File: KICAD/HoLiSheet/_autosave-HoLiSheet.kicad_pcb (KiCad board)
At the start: 2 copper layers, 22.4 x 31.4 mm, 13 parts, among them J1 Conn_01x06, J2 Conn_01x01_Male, J3 Conn_01x06, J4 Conn_01x01_Male, J5 Conn_01x01_Male, J6 Conn_01x01_Male, J7 Conn_01x01_Male, J8 Conn_01x01_Male

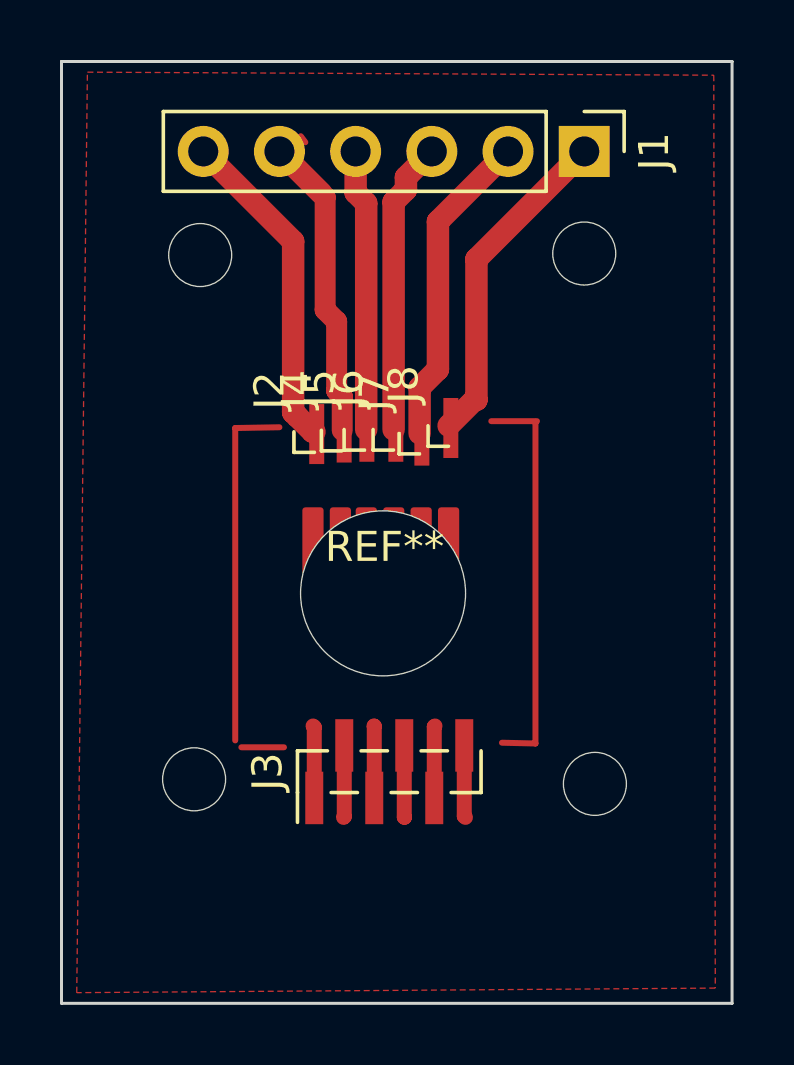
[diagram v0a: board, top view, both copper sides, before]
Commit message: Adding new standalone CAD and new iamges
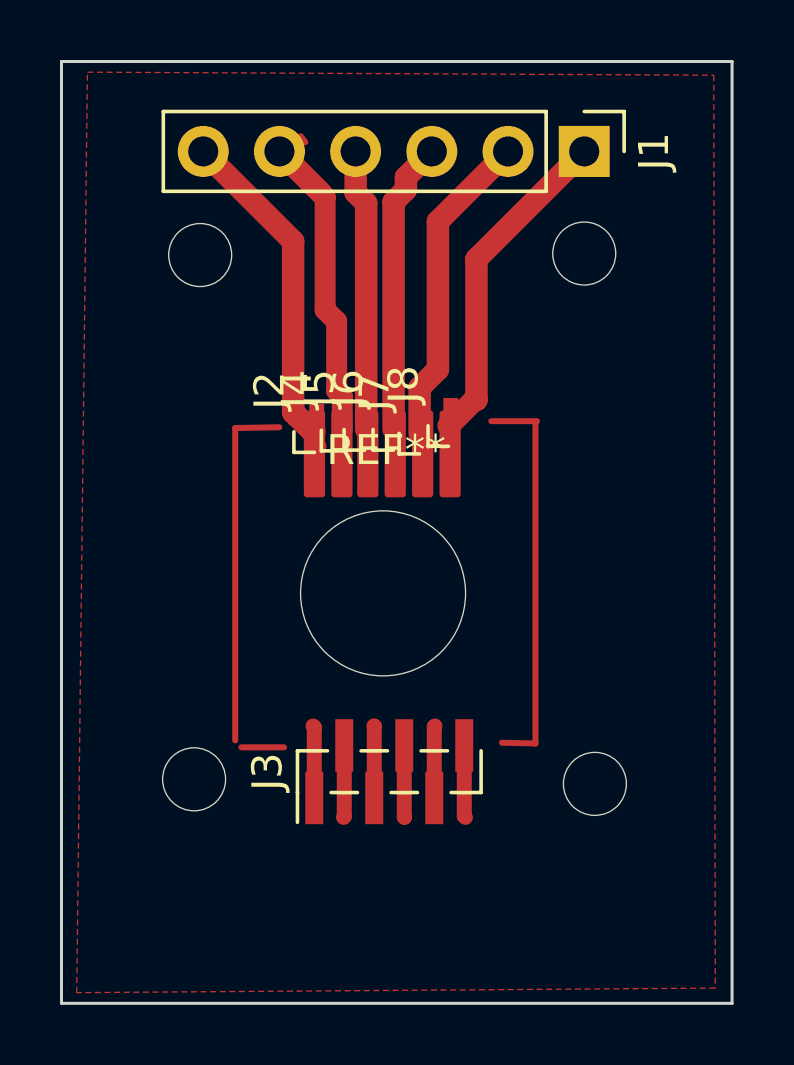
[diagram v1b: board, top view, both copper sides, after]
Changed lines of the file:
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@@
     (tags "mounting hole 5.5mm no annular")
     (attr exclude_from_pos_files exclude_from_bom)
-    (fp_text reference "REF**" (at 0.0508 -1.547) (layer "F.SilkS")
+    (fp_text reference "REF**" (at 0.1016 -4.7728) (layer "F.SilkS")
       (effects (font (size 1 1) (thickness 0.15)))
     )
@@
   (gr_line (start 16.002 12.1666) (end 16.002 22.8854) (layer "F.Cu") (width 0.2))
   (gr_line (start 16.002 22.8854) (end 14.8844 22.86) (layer "F.Cu") (width 0.2))
-  (gr_rect (start 10.6172 15.113) (end 10.1092 17.8054) (layer "F.Cu") (width 0.2) (fill solid))
-  (gr_rect (start 12.446 15.113) (end 11.938 17.8054) (layer "F.Cu") (width 0.2) (fill solid))
-  (gr_rect (start 9.7536 15.113) (end 9.2456 17.8054) (layer "F.Cu") (width 0.2) (fill solid))
+  (gr_rect (start 10.668 11.8872) (end 10.16 14.5796) (layer "F.Cu") (width 0.2) (fill solid))
+  (gr_rect (start 12.4968 11.8872) (end 11.9888 14.5796) (layer "F.Cu") (width 0.2) (fill solid))
+  (gr_rect (start 9.8044 11.8872) (end 9.2964 14.5796) (layer "F.Cu") (width 0.2) (fill solid))
   (gr_line (start 6.1976 23.0124) (end 7.62 23.0124) (layer "F.Cu") (width 0.2))
   (gr_line (start 5.9944 12.3698) (end 5.9944 22.7838) (layer "F.Cu") (width 0.2))
-  (gr_rect (start 11.5316 15.113) (end 11.0236 17.8054) (layer "F.Cu") (width 0.2) (fill solid))
-  (gr_rect (start 13.3604 15.113) (end 12.8524 17.8054) (layer "F.Cu") (width 0.2) (fill solid))
+  (gr_rect (start 11.5824 11.8872) (end 11.0744 14.5796) (layer "F.Cu") (width 0.2) (fill solid))
+  (gr_rect (start 13.4112 11.8872) (end 12.9032 14.5796) (layer "F.Cu") (width 0.2) (fill solid))
   (gr_line (start 8.1788 2.6416) (end 8.3312 2.8448) (layer "F.Cu") (width 0.2))
-  (gr_rect (start 8.8392 15.113) (end 8.3312 17.8054) (layer "F.Cu") (width 0.2) (fill solid))
+  (gr_rect (start 8.89 11.8872) (end 8.382 14.5796) (layer "F.Cu") (width 0.2) (fill solid))
   (gr_line (start 7.4676 12.3444) (end 5.9944 12.3698) (layer "F.Cu") (width 0.2))
   (gr_line (start 0.2032 0.1524) (end 0.6096 0.1524) (layer "Edge.Cuts") (width 0.1))
@@
   (segment (start 8.578317 12.4968) (end 8.636 12.4968) (width 0.75) (layer "F.Cu") (net 6))
   (segment (start 4.9276 3.1496) (end 7.9248 6.1468) (width 0.75) (layer "F.Cu") (net 6))
-  (segment (start 8.7376 16.2052) (end 8.636 16.3068) (width 0.5) (layer "F.Cu") (net 6))
+  (segment (start 8.7884 12.9794) (end 8.6868 13.081) (width 0.5) (layer "F.Cu") (net 6))
   (segment (start 8.070317 11.9888) (end 8.578317 12.4968) (width 0.75) (layer "F.Cu") (net 6))
   (segment (start 7.9248 6.1468) (end 7.9248 11.848216) (width 0.75) (layer "F.Cu") (net 6))
